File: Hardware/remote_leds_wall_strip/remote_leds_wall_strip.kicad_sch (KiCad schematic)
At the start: 18 parts, among them J1 Conn_01x02_Male

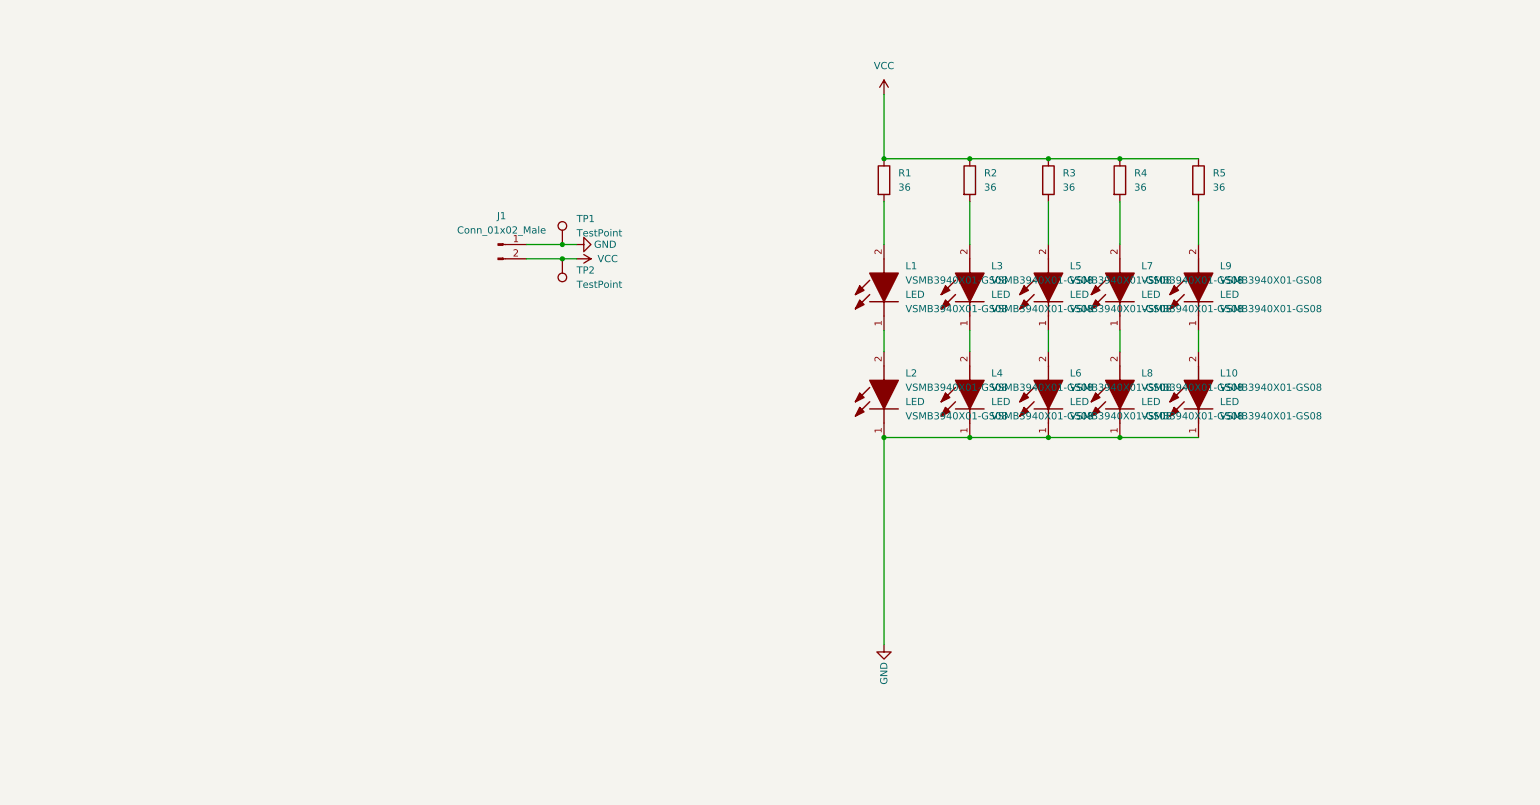
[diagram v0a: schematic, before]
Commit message: upgrade wall led strip from 20cm to 50cm
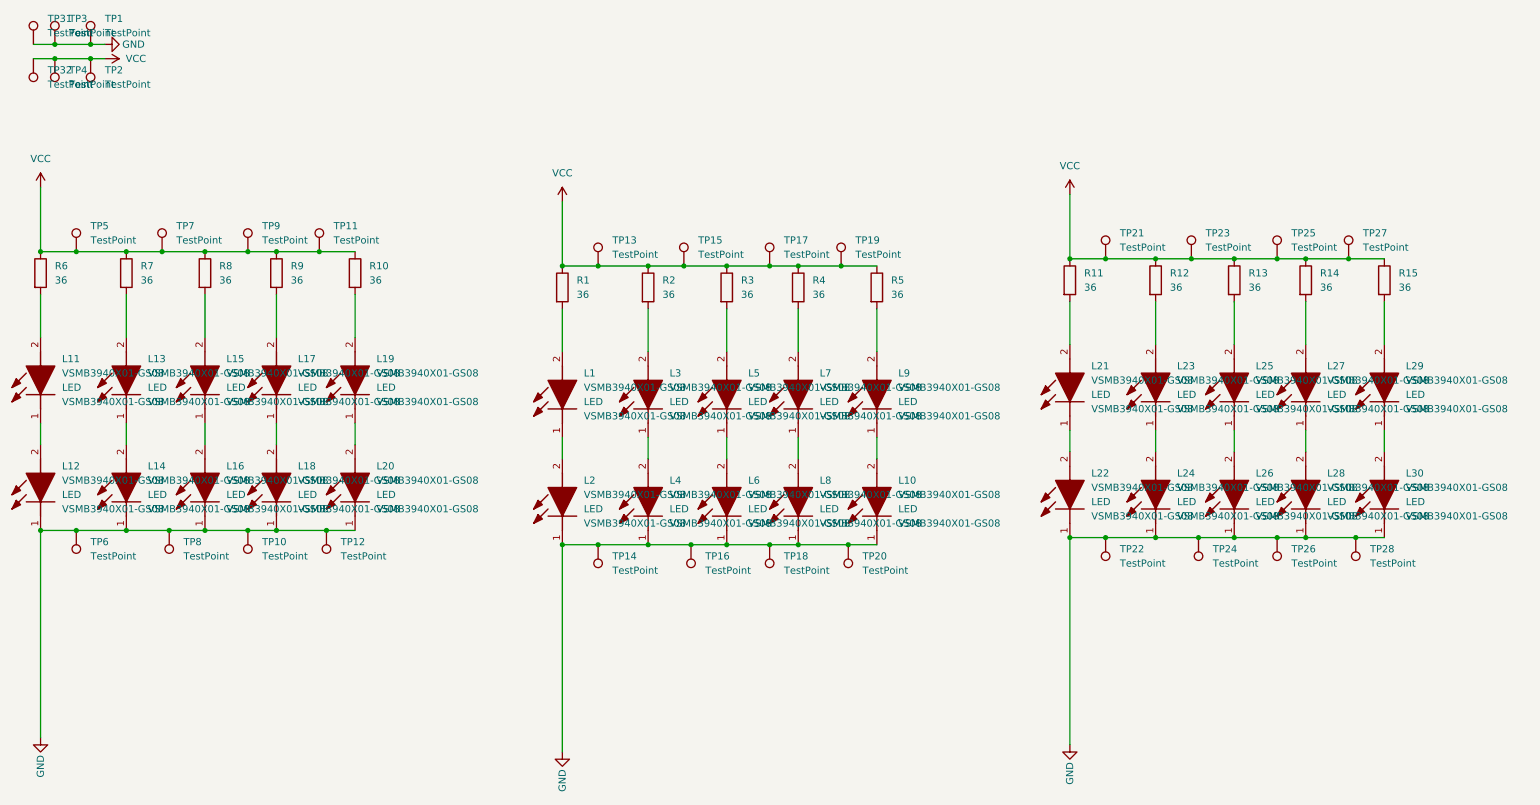
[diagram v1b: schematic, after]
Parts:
- removed J1: Conn_01x02_Male, Connector_PinHeader_2.54mm:PinHeader_1x02_P2.54mm_Vertical, symbol Connector:Conn_01x02_Male
- added L11, L12, L13, L14, L15, L16, L17, L18, L19, L20, L21, L22, L23, L24, L25, L26, L27, L28, L29, L30: VSMB3940X01-GS08, Footprints:LEDM3528X185N, symbol VSMB3940X01-GS08:VSMB3940X01-GS08
- added R10, R11, R12, R13, R14, R15, R6, R7, R8, R9: 36, Resistor_SMD:R_0805_2012Metric_Pad1.20x1.40mm_HandSolder, symbol Device:R
- added TP10, TP11, TP12, TP13, TP14, TP15, TP16, TP17, TP18, TP19, TP20, TP21, TP22, TP23, TP24, TP25, TP26, TP27, TP28, TP3, TP31, TP32, TP4, TP5, TP6, TP7, TP8, TP9: TestPoint, TestPoint:TestPoint_Pad_2.5x2.5mm, symbol Connector:TestPoint
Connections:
- net GND: now also L12.1 (K), L14.1 (K), L16.1 (K), L18.1 (K), L20.1 (K), L22.1 (K), L24.1 (K), L26.1 (K), L28.1 (K), L30.1 (K), TP10.1, TP12.1, TP14.1, TP16.1, TP18.1, TP20.1, TP22.1, TP24.1, TP26.1, TP28.1, TP3.1, TP31.1, TP6.1, TP8.1
- net VCC: now also R10.1, R11.1, R12.1, R13.1, R14.1, R15.1, R6.1, R7.1, R8.1, R9.1, TP11.1, TP13.1, TP15.1, TP17.1, TP19.1, TP21.1, TP23.1, TP25.1, TP27.1, TP32.1, TP4.1, TP5.1, TP7.1, TP9.1
- new net: L23.1 (K), L24.2 (A)
- new net: L23.2 (A), R12.2
- new net: L13.1 (K), L14.2 (A)
- new net: L13.2 (A), R7.2
- new net: L29.1 (K), L30.2 (A)
- new net: L19.2 (A), R10.2
- new net: L17.1 (K), L18.2 (A)
- new net: L17.2 (A), R9.2
- new net: L25.2 (A), R13.2
- new net: L29.2 (A), R15.2
- new net: L21.1 (K), L22.2 (A)
- new net: L11.2 (A), R6.2
- new net: L11.1 (K), L12.2 (A)
- new net: L19.1 (K), L20.2 (A)
- new net: L25.1 (K), L26.2 (A)
- new net: L15.1 (K), L16.2 (A)
- new net: L15.2 (A), R8.2
- new net: L27.1 (K), L28.2 (A)
- new net: L27.2 (A), R14.2
- new net: L21.2 (A), R11.2
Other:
- moved on the sheet: L1, L10, L2, L3, L4, L5, L6, L7, L8, L9, R1, R2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

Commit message: changing the size of the strip led from 50 to 30cm
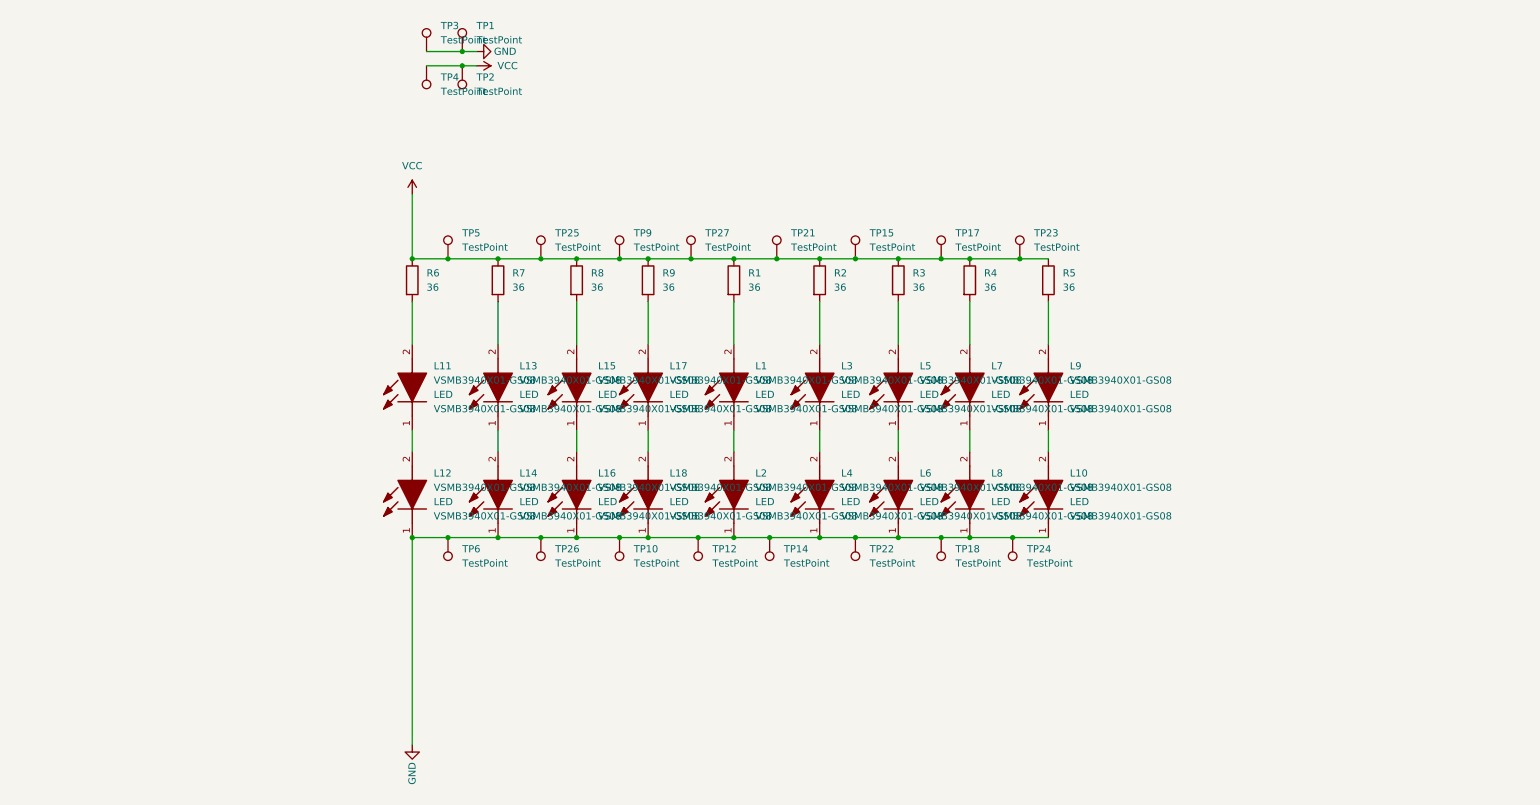
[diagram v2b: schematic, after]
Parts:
- removed L19, L20, L21, L22, L23, L24, L25, L26, L27, L28, L29, L30: VSMB3940X01-GS08, Footprints:LEDM3528X185N, symbol VSMB3940X01-GS08:VSMB3940X01-GS08
- removed R10, R11, R12, R13, R14, R15: 36, Resistor_SMD:R_0805_2012Metric_Pad1.20x1.40mm_HandSolder, symbol Device:R
- removed TP11, TP13, TP16, TP19, TP20, TP28, TP31, TP32, TP7, TP8: TestPoint, TestPoint:TestPoint_Pad_2.5x2.5mm, symbol Connector:TestPoint
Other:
- moved on the sheet: L1, L10, L11, L12, L13, L14, L15, L16, L17, L18, L2, L3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

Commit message: update resistance values
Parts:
- R1, R2, R3, R4, R5, R6, R7, R8, R9: value 36 -> 15
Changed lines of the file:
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@@
       (effects (font (size 1.27 1.27)) (justify left))
     )
-    (property "Value" "36" (id 1) (at 161.29 67.3099 0)
+    (property "Value" "15" (id 1) (at 161.29 67.3099 0)
       (effects (font (size 1.27 1.27)) (justify left))
     )
@@
       (effects (font (size 1.27 1.27)) (justify left))
     )
-    (property "Value" "36" (id 1) (at 146.05 67.3099 0)
+    (property "Value" "15" (id 1) (at 146.05 67.3099 0)
       (effects (font (size 1.27 1.27)) (justify left))
     )
@@
       (effects (font (size 1.27 1.27)) (justify left))
     )
-    (property "Value" "36" (id 1) (at 130.81 67.3099 0)
+    (property "Value" "15" (id 1) (at 130.81 67.3099 0)
       (effects (font (size 1.27 1.27)) (justify left))
     )
@@
       (effects (font (size 1.27 1.27)) (justify left))
     )
-    (property "Value" "36" (id 1) (at 88.9 67.3099 0)
+    (property "Value" "15" (id 1) (at 88.9 67.3099 0)
       (effects (font (size 1.27 1.27)) (justify left))
     )
@@
       (effects (font (size 1.27 1.27)) (justify left))
     )
-    (property "Value" "36" (id 1) (at 201.93 67.3099 0)
+    (property "Value" "15" (id 1) (at 201.93 67.3099 0)
       (effects (font (size 1.27 1.27)) (justify left))
     )
@@
       (effects (font (size 1.27 1.27)) (justify left))
     )
-    (property "Value" "36" (id 1) (at 175.26 67.3099 0)
+    (property "Value" "15" (id 1) (at 175.26 67.3099 0)
       (effects (font (size 1.27 1.27)) (justify left))
     )
@@
       (effects (font (size 1.27 1.27)) (justify left))
     )
-    (property "Value" "36" (id 1) (at 187.96 67.3099 0)
+    (property "Value" "15" (id 1) (at 187.96 67.3099 0)
       (effects (font (size 1.27 1.27)) (justify left))
     )
@@
       (effects (font (size 1.27 1.27)) (justify left))
     )
-    (property "Value" "36" (id 1) (at 104.14 67.3099 0)
+    (property "Value" "15" (id 1) (at 104.14 67.3099 0)
       (effects (font (size 1.27 1.27)) (justify left))
     )
@@
       (effects (font (size 1.27 1.27)) (justify left))
     )
-    (property "Value" "36" (id 1) (at 118.11 67.3099 0)
+    (property "Value" "15" (id 1) (at 118.11 67.3099 0)
       (effects (font (size 1.27 1.27)) (justify left))
     )
@@
     )
     (path "/4010410d-6e12-47b9-8899-68b22e8bb971"
-      (reference "R1") (unit 1) (value "36") (footprint "Resistor_SMD:R_0805_2012Metric_Pad1.20x1.40mm_HandSolder")
+      (reference "R1") (unit 1) (value "15") (footprint "Resistor_SMD:R_0805_2012Metric_Pad1.20x1.40mm_HandSolder")
     )
     (path "/11132bf4-7c00-42c9-81d9-f1557de6d30f"
-      (reference "R2") (unit 1) (value "36") (footprint "Resistor_SMD:R_0805_2012Metric_Pad1.20x1.40mm_HandSolder")
+      (reference "R2") (unit 1) (value "15") (footprint "Resistor_SMD:R_0805_2012Metric_Pad1.20x1.40mm_HandSolder")
     )
     (path "/7ee5b50d-e917-420e-93f0-f3f70a7cbfc1"
-      (reference "R3") (unit 1) (value "36") (footprint "Resistor_SMD:R_0805_2012Metric_Pad1.20x1.40mm_HandSolder")
+      (reference "R3") (unit 1) (value "15") (footprint "Resistor_SMD:R_0805_2012Metric_Pad1.20x1.40mm_HandSolder")
     )
     (path "/9f533b3f-86a3-4fc2-b4f9-e39e32db94a6"
-      (reference "R4") (unit 1) (value "36") (footprint "Resistor_SMD:R_0805_2012Metric_Pad1.20x1.40mm_HandSolder")
+      (reference "R4") (unit 1) (value "15") (footprint "Resistor_SMD:R_0805_2012Metric_Pad1.20x1.40mm_HandSolder")
     )
     (path "/7ab03e41-3189-4e93-b727-b7c20efb3426"
-      (reference "R5") (unit 1) (value "36") (footprint "Resistor_SMD:R_0805_2012Metric_Pad1.20x1.40mm_HandSolder")
+      (reference "R5") (unit 1) (value "15") (footprint "Resistor_SMD:R_0805_2012Metric_Pad1.20x1.40mm_HandSolder")
     )
     (path "/582a9be5-9d2d-4ac4-9cca-3a64691d73eb"
-      (reference "R6") (unit 1) (value "36") (footprint "Resistor_SMD:R_0805_2012Metric_Pad1.20x1.40mm_HandSolder")
+      (reference "R6") (unit 1) (value "15") (footprint "Resistor_SMD:R_0805_2012Metric_Pad1.20x1.40mm_HandSolder")
     )
     (path "/dec4c151-2606-4aa5-bd29-b53a50648782"
-      (reference "R7") (unit 1) (value "36") (footprint "Resistor_SMD:R_0805_2012Metric_Pad1.20x1.40mm_HandSolder")
+      (reference "R7") (unit 1) (value "15") (footprint "Resistor_SMD:R_0805_2012Metric_Pad1.20x1.40mm_HandSolder")
     )
     (path "/e6e36fe4-5a0b-49d5-ab27-515be59ed115"
-      (reference "R8") (unit 1) (value "36") (footprint "Resistor_SMD:R_0805_2012Metric_Pad1.20x1.40mm_HandSolder")
+      (reference "R8") (unit 1) (value "15") (footprint "Resistor_SMD:R_0805_2012Metric_Pad1.20x1.40mm_HandSolder")
     )
     (path "/4a74bd16-a911-4bd5-9c24-401feabea144"
-      (reference "R9") (unit 1) (value "36") (footprint "Resistor_SMD:R_0805_2012Metric_Pad1.20x1.40mm_HandSolder")
+      (reference "R9") (unit 1) (value "15") (footprint "Resistor_SMD:R_0805_2012Metric_Pad1.20x1.40mm_HandSolder")
     )
     (path "/24686760-1acf-4676-81e5-d7de0f146a00"
